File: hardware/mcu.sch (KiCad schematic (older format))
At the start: 29 parts, among them J1 Micro_SD_Card, J2 BOOT0, J3 Conn_01x04_Male, J5 Conn_01x03_Male, J6 display, SW1 SW_right, SW2 SW_right, SW3 SW_top, SW4 SW_middle, SW5 SW_bot, SW6 SW_Left, SW7 SW_middle2, U1 STM32F042C6Tx

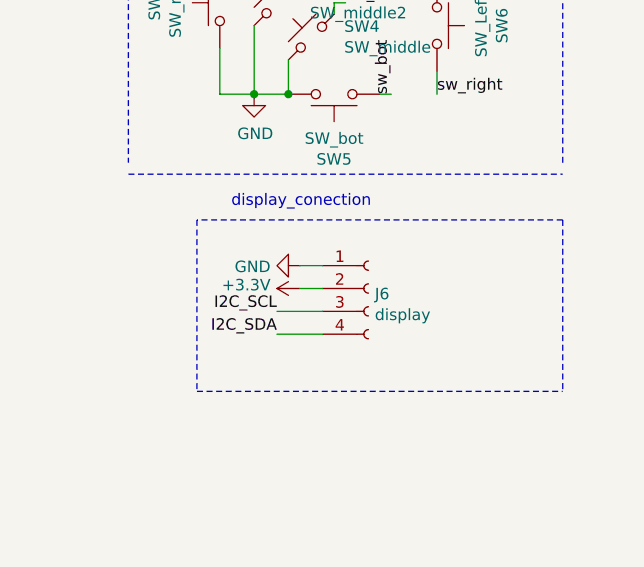
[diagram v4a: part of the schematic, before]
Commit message: Dodenie pullup do spi i i2c
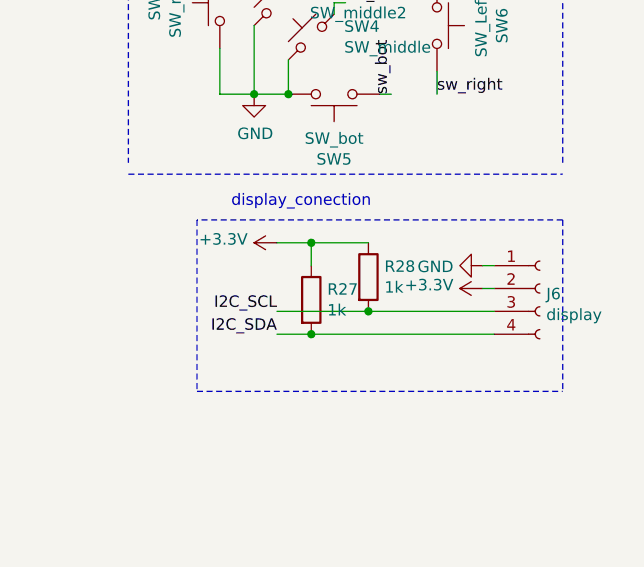
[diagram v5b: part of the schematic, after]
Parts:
- added R27, R28: 1k, Resistor_SMD:R_0603_1608Metric_Pad1.05x0.95mm_HandSolder, symbol Device:R
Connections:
- net +3V3: now also R27.1, R28.1
- net I2C_SCL: now also R28.2
- net I2C_SDA: now also R27.2
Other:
- moved on the sheet: J6
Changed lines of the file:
@@
 L power:GND #PWR?
 U 1 1 5D235C25
-P 8650 4700
+P 9450 4700
 AR Path="/5CDEAC68/5D235C25" Ref="#PWR?"  Part="1"
 AR Path="/5CDEAB6D/5D235C25" Ref="#PWR0139"  Part="1"
-F 0 "#PWR0139" H 8650 4450 50  0001 C CNN
-F 1 "GND" V 8655 4572 50  0000 R CNN
-F 2 "" H 8650 4700 50  0001 C CNN
-F 3 "" H 8650 4700 50  0001 C CNN
-	1    8650 4700
+F 0 "#PWR0139" H 9450 4450 50  0001 C CNN
+F 1 "GND" V 9455 4572 50  0000 R CNN
+F 2 "" H 9450 4700 50  0001 C CNN
+F 3 "" H 9450 4700 50  0001 C CNN
+	1    9450 4700
 	0    1    1    0
-$EndComp
-$Comp
-L power:+3.3V #PWR?
-U 1 1 5D235C2B
-P 8650 4800
-AR Path="/5CDEAC68/5D235C2B" Ref="#PWR?"  Part="1"
-AR Path="/5CDEAB6D/5D235C2B" Ref="#PWR0141"  Part="1"
-F 0 "#PWR0141" H 8650 4650 50  0001 C CNN
-F 1 "+3.3V" V 8665 4928 50  0000 L CNN
-F 2 "" H 8650 4800 50  0001 C CNN
-F 3 "" H 8650 4800 50  0001 C CNN
-	1    8650 4800
-	0    -1   -1   0
 $EndComp
 Text Label 8550 4900 2    50   ~ 0
@@
 L Connector:Conn_01x04_Female J6
 U 1 1 5D24C80E
-P 8950 4800
-F 0 "J6" H 8978 4776 50  0000 L CNN
-F 1 "display" H 8978 4685 50  0000 L CNN
-F 2 "Connector_PinSocket_2.54mm:PinSocket_1x04_P2.54mm_Vertical" H 8950 4800 50  0001 C CNN
-F 3 "~" H 8950 4800 50  0001 C CNN
-	1    8950 4800
+P 9700 4800
+F 0 "J6" H 9728 4776 50  0000 L CNN
+F 1 "display" H 9728 4685 50  0000 L CNN
+F 2 "Connector_PinSocket_2.54mm:PinSocket_1x04_P2.54mm_Vertical" H 9700 4800 50  0001 C CNN
+F 3 "~" H 9700 4800 50  0001 C CNN
+	1    9700 4800
 	1    0    0    -1
 $EndComp
 Wire Wire Line
-	8550 4900 8750 4900
+	9450 4700 9500 4700
 Wire Wire Line
-	8750 4800 8650 4800
-Wire Wire Line
-	8650 4700 8750 4700
-Wire Wire Line
-	8750 5000 8550 5000
+	9500 5000 8700 5000
 Text Notes 8350 4450 0    50   ~ 0
 display_conection
@@
 Text Notes 1500 3000 0    50   ~ 0
 programing connection\n
+Wire Wire Line
+	9500 4800 9450 4800
+$Comp
+L power:+3.3V #PWR?
+U 1 1 5D235C2B
+P 9450 4800
+AR Path="/5CDEAC68/5D235C2B" Ref="#PWR?"  Part="1"
+AR Path="/5CDEAB6D/5D235C2B" Ref="#PWR0141"  Part="1"
+F 0 "#PWR0141" H 9450 4650 50  0001 C CNN
+F 1 "+3.3V" V 9465 4928 50  0000 L CNN
+F 2 "" H 9450 4800 50  0001 C CNN
+F 3 "" H 9450 4800 50  0001 C CNN
+	1    9450 4800
+	0    -1   -1   0
+$EndComp
+$Comp
+L Device:R R27
+U 1 1 5D3198A1
+P 8700 4850
+F 0 "R27" H 8770 4896 50  0000 L CNN
+F 1 "1k" H 8770 4805 50  0000 L CNN
+F 2 "Resistor_SMD:R_0603_1608Metric_Pad1.05x0.95mm_HandSolder" V 8630 4850 50  0001 C CNN
+F 3 "~" H 8700 4850 50  0001 C CNN
+	1    8700 4850
+	1    0    0    -1
+$EndComp
+Connection ~ 8700 5000
+Wire Wire Line
+	8700 5000 8550 5000
+$Comp
+L Device:R R28
+U 1 1 5D319E5F
+P 8950 4750
+F 0 "R28" H 9020 4796 50  0000 L CNN
+F 1 "1k" H 9020 4705 50  0000 L CNN
+F 2 "Resistor_SMD:R_0603_1608Metric_Pad1.05x0.95mm_HandSolder" V 8880 4750 50  0001 C CNN
+F 3 "~" H 8950 4750 50  0001 C CNN
+	1    8950 4750
+	1    0    0    -1
+$EndComp
+$Comp
+L power:+3.3V #PWR?
+U 1 1 5D31ED2B
+P 8550 4600
+AR Path="/5CDEAC68/5D31ED2B" Ref="#PWR?"  Part="1"
+AR Path="/5CDEAB6D/5D31ED2B" Ref="#PWR0142"  Part="1"
+F 0 "#PWR0142" H 8550 4450 50  0001 C CNN
+F 1 "+3.3V" V 8565 4728 50  0000 L CNN
+F 2 "" H 8550 4600 50  0001 C CNN
+F 3 "" H 8550 4600 50  0001 C CNN
+	1    8550 4600
+	0    -1   -1   0
+$EndComp
+Wire Wire Line
+	8550 4600 8700 4600
+Wire Wire Line
+	8700 4700 8700 4600
+Connection ~ 8700 4600
+Connection ~ 8950 4900
+Wire Wire Line
+	8950 4900 9500 4900
+Wire Wire Line
+	8550 4900 8950 4900
+Wire Wire Line
+	8700 4600 8950 4600
 $EndSCHEMATC

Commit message: pierwszy układ PCB
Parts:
- added R32, R33: 47, Resistor_SMD:R_0603_1608Metric_Pad1.05x0.95mm_HandSolder, symbol Device:R
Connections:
- net POTMOSI: now also R33.2; no longer U1.41 (PB5)
- net POTSCK: now also R32.2; no longer U1.39 (PB3)
- new net: R32.1, U1.39 (PB3)
- new net: R33.1, U1.41 (PB5)
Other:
- moved on the sheet: R27, R28
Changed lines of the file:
@@
 Wire Wire Line
 	5250 5300 4900 5300
-Text HLabel 4800 4100 0    50   Output ~ 0
+Text HLabel 4400 4100 0    50   Output ~ 0
 POTSCK
-Text HLabel 4800 4300 0    50   Output ~ 0
-POTMOSI
-Wire Wire Line
-	4800 4100 5250 4100
-Wire Wire Line
-	5250 4300 4800 4300
-Text Label 4900 4100 0    50   ~ 0
-POTSCK
-Text Label 4900 4300 0    50   ~ 0
+Text HLabel 4400 4300 0    50   Output ~ 0
 POTMOSI
 Text Label 4950 4200 0    50   ~ 0
 POTSS
 Wire Wire Line
-	5250 4200 4800 4200
-Text HLabel 4800 4200 0    50   Output ~ 0
+	5250 4200 4400 4200
+Text HLabel 4400 4200 0    50   Output ~ 0
 POTCS
 Wire Wire Line
@@
 ADC6
 Wire Wire Line
-	5250 4400 4850 4400
-Wire Wire Line
-	5250 4500 4850 4500
-Text HLabel 4850 4400 0    50   Output ~ 0
+	5250 4400 4400 4400
+Wire Wire Line
+	5250 4500 4400 4500
+Text HLabel 4400 4400 0    50   Output ~ 0
 POTRST
 Text Label 4950 4400 0    50   ~ 0
@@
 	0    1    1    0
 $EndComp
-Text HLabel 4850 4500 0    50   Output ~ 0
+Text HLabel 4400 4500 0    50   Output ~ 0
 POTSHDN
 Wire Wire Line
@@
 	9450 4700 9500 4700
 Wire Wire Line
-	9500 5000 8700 5000
+	9500 5000 8650 5000
 Text Notes 8350 4450 0    50   ~ 0
 display_conection
@@
 	0    -1   -1   0
 $EndComp
-$Comp
-L Device:R R27
-U 1 1 5D3198A1
-P 8700 4850
-F 0 "R27" H 8770 4896 50  0000 L CNN
-F 1 "1k" H 8770 4805 50  0000 L CNN
-F 2 "Resistor_SMD:R_0603_1608Metric_Pad1.05x0.95mm_HandSolder" V 8630 4850 50  0001 C CNN
-F 3 "~" H 8700 4850 50  0001 C CNN
-	1    8700 4850
-	1    0    0    -1
-$EndComp
-Connection ~ 8700 5000
-Wire Wire Line
-	8700 5000 8550 5000
+Connection ~ 8650 5000
 $Comp
 L Device:R R28
 U 1 1 5D319E5F
-P 8950 4750
-F 0 "R28" H 9020 4796 50  0000 L CNN
-F 1 "1k" H 9020 4705 50  0000 L CNN
-F 2 "Resistor_SMD:R_0603_1608Metric_Pad1.05x0.95mm_HandSolder" V 8880 4750 50  0001 C CNN
-F 3 "~" H 8950 4750 50  0001 C CNN
-	1    8950 4750
+P 8900 4750
+F 0 "R28" H 8970 4796 50  0000 L CNN
+F 1 "1k" H 8970 4705 50  0000 L CNN
+F 2 "Resistor_SMD:R_0603_1608Metric_Pad1.05x0.95mm_HandSolder" V 8830 4750 50  0001 C CNN
+F 3 "~" H 8900 4750 50  0001 C CNN
+	1    8900 4750
 	1    0    0    -1
 $EndComp
@@
 $EndComp
 Wire Wire Line
-	8550 4600 8700 4600
-Wire Wire Line
-	8700 4700 8700 4600
-Connection ~ 8700 4600
-Connection ~ 8950 4900
-Wire Wire Line
-	8950 4900 9500 4900
-Wire Wire Line
-	8550 4900 8950 4900
-Wire Wire Line
-	8700 4600 8950 4600
+	8550 4600 8650 4600
+Wire Wire Line
+	8650 4700 8650 4600
+Connection ~ 8650 4600
+Connection ~ 8900 4900
+Wire Wire Line
+	8900 4900 9500 4900
+Wire Wire Line
+	8550 4900 8900 4900
+Wire Wire Line
+	8650 4600 8900 4600
+$Comp
+L Device:R R32
+U 1 1 5D460BB7
+P 4700 4100
+F 0 "R32" V 4493 4100 50  0000 C CNN
+F 1 "47" V 4584 4100 50  0000 C CNN
+F 2 "Resistor_SMD:R_0603_1608Metric_Pad1.05x0.95mm_HandSolder" V 4630 4100 50  0001 C CNN
+F 3 "~" H 4700 4100 50  0001 C CNN
+	1    4700 4100
+	0    1    1    0
+$EndComp
+$Comp
+L Device:R R33
+U 1 1 5D4611CB
+P 4700 4300
+F 0 "R33" V 4493 4300 50  0000 C CNN
+F 1 "47" V 4584 4300 50  0000 C CNN
+F 2 "Resistor_SMD:R_0603_1608Metric_Pad1.05x0.95mm_HandSolder" V 4630 4300 50  0001 C CNN
+F 3 "~" H 4700 4300 50  0001 C CNN
+	1    4700 4300
+	0    1    1    0
+$EndComp
+Wire Wire Line
+	4400 4300 4550 4300
+Wire Wire Line
+	4400 4100 4550 4100
+Wire Wire Line
+	4850 4100 5250 4100
+Wire Wire Line
+	5250 4300 4850 4300
+Wire Wire Line
+	8650 5000 8550 5000
+$Comp
+L Device:R R27
+U 1 1 5D3198A1
+P 8650 4850
+F 0 "R27" H 8720 4896 50  0000 L CNN
+F 1 "1k" H 8720 4805 50  0000 L CNN
+F 2 "Resistor_SMD:R_0603_1608Metric_Pad1.05x0.95mm_HandSolder" V 8580 4850 50  0001 C CNN
+F 3 "~" H 8650 4850 50  0001 C CNN
+	1    8650 4850
+	1    0    0    -1
+$EndComp
 $EndSCHEMATC

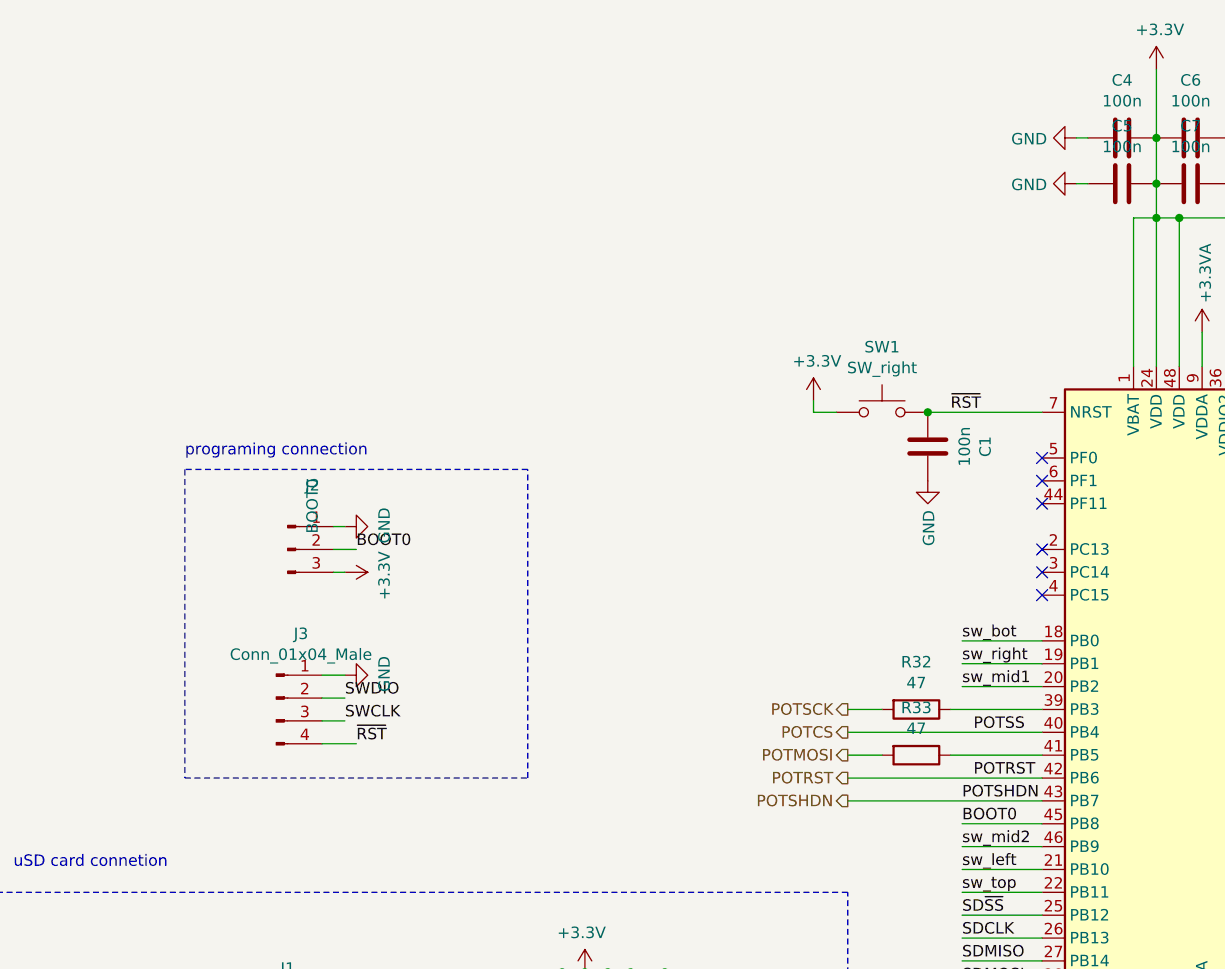
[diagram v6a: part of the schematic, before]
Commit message: update pinoutu, zmiany footprintów
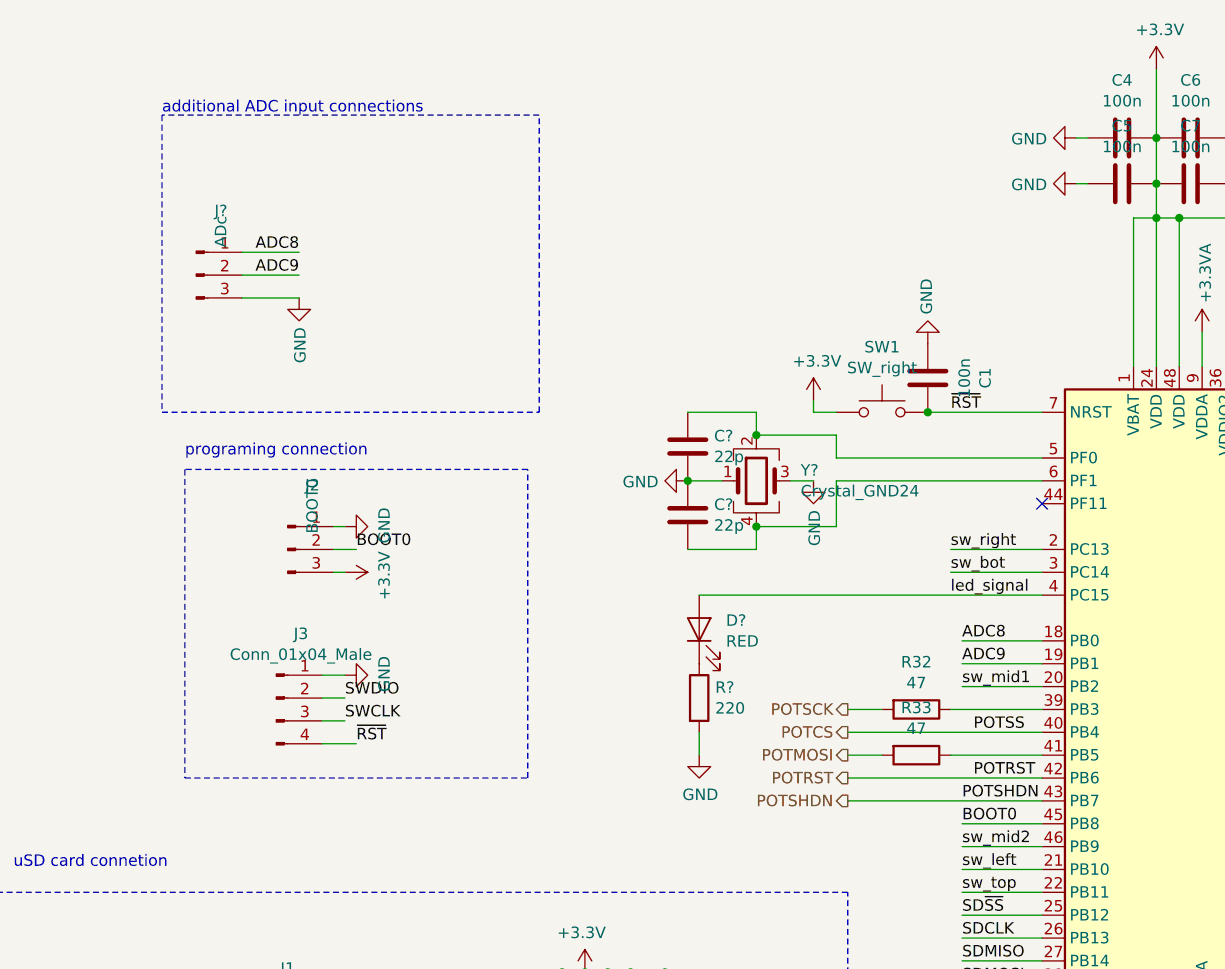
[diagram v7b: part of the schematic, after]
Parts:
- added C? (x2): 22p, symbol Device:C
- added D?: RED, LED_SMD:LED_0805_2012Metric, symbol Device:LED
- added J?: ADc, Connector_PinHeader_2.54mm:PinHeader_1x03_P2.54mm_Vertical, symbol Connector:Conn_01x03_Male
- added R?: 220, Resistor_SMD:R_0603_1608Metric_Pad1.05x0.95mm_HandSolder, symbol Device:R
- added Y?: Crystal_GND24, symbol Device:Crystal_GND24
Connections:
- net GND: now also C1.2, C?.1, C?.2, J?.3 (Pin_3), R?.2, Y?.1, Y?.3; no longer C1.1
- net sw_bot: now also U1.3 (PC14); no longer U1.18 (PB0)
- net sw_right: now also U1.2 (PC13); no longer U1.19 (PB1)
- net ~RST: now also C1.1; no longer C1.2
- net led_signal: now reaches U1.4 (PC15)
- net led_signal: now also D?.2 (A)
- net at U1.5 (PF0): now also C?.1, Y?.2
- net at U1.6 (PF1): now also C?.2, Y?.4
- new net: D?.1 (K), R?.1
- new net ADC8: J?.1 (Pin_1), U1.18 (PB0)
- new net ADC9: J?.2 (Pin_2), U1.19 (PB1)
- no-connect marks 7 -> 2
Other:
- note added: "additional ADC input connections\n"
- moved on the sheet: C1
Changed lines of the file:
@@
 	4100 6250 3600 6250
 Connection ~ 3600 6250
-$Comp
-L MCU_ST_STM32F0:STM32F042C6Tx U1
-U 1 1 5D61AD1D
-P 5850 4000
-F 0 "U1" H 5850 2411 50  0000 C CNN
-F 1 "STM32F042C6Tx" H 5850 2320 50  0000 C CNN
-F 2 "Package_QFP:LQFP-48_7x7mm_P0.5mm" H 5350 2600 50  0001 R CNN
-F 3 "http://www.st.com/st-web-ui/static/active/en/resource/technical/document/datasheet/DM00105814.pdf" H 5850 4000 50  0001 C CNN
-	1    5850 4000
-	1    0    0    -1
-$EndComp
 Wire Wire Line
 	5650 2600 5650 1950
@@
 Text Label 6500 4500 0    50   ~ 0
 ADC7
-Text HLabel 6700 3800 2    50   Output ~ 0
-ADC0
 Text HLabel 6700 3900 2    50   Output ~ 0
 ADC1
@@
 Text Label 4900 4000 0    50   ~ 0
 sw_mid1
-Text Label 4900 3900 0    50   ~ 0
+Text Label 4850 3400 0    50   ~ 0
 sw_right
-Text Label 4900 3800 0    50   ~ 0
+Text Label 4850 3500 0    50   ~ 0
 sw_bot
 $Comp
 L Device:C C1
 U 1 1 5CE5A2EA
-P 4750 2950
-F 0 "C1" V 4498 2950 50  0000 C CNN
-F 1 "100n" V 4589 2950 50  0000 C CNN
-F 2 "Capacitor_SMD:C_0603_1608Metric_Pad1.05x0.95mm_HandSolder" H 4788 2800 50  0001 C CNN
-F 3 "~" H 4750 2950 50  0001 C CNN
-	1    4750 2950
+P 4750 2650
+F 0 "C1" V 4498 2650 50  0000 C CNN
+F 1 "100n" V 4589 2650 50  0000 C CNN
+F 2 "Capacitor_SMD:C_0603_1608Metric_Pad1.05x0.95mm_HandSolder" H 4788 2500 50  0001 C CNN
+F 3 "~" H 4750 2650 50  0001 C CNN
+	1    4750 2650
 	-1   0    0    1
 $EndComp
@@
 L power:GND #PWR08
 U 1 1 5CE5FAB4
-P 4750 3100
-F 0 "#PWR08" H 4750 2850 50  0001 C CNN
-F 1 "GND" V 4755 2972 50  0000 R CNN
-F 2 "" H 4750 3100 50  0001 C CNN
-F 3 "" H 4750 3100 50  0001 C CNN
-	1    4750 3100
-	1    0    0    -1
+P 4750 2500
+F 0 "#PWR08" H 4750 2250 50  0001 C CNN
+F 1 "GND" V 4755 2372 50  0000 R CNN
+F 2 "" H 4750 2500 50  0001 C CNN
+F 3 "" H 4750 2500 50  0001 C CNN
+	1    4750 2500
+	-1   0    0    1
 $EndComp
 Text Label 4850 2800 0    50   ~ 0
@@
 	1    0    0    -1
 $EndComp
-Connection ~ 4750 2800
 $Comp
 L power:+3.3V #PWR07
@@
 Wire Wire Line
 	6450 4900 6850 4900
-NoConn ~ 5250 3000
-NoConn ~ 5250 3100
 NoConn ~ 5250 3200
-NoConn ~ 5250 3400
-NoConn ~ 5250 3500
-NoConn ~ 5250 3600
 $Comp
 L power:GNDA #PWR022
@@
 	1    0    0    -1
 $EndComp
+Text HLabel 6700 3800 2    50   Output ~ 0
+ADC0
+Text Label 4900 3800 0    50   ~ 0
+ADC8
+Text Label 4900 3900 0    50   ~ 0
+ADC9
+Wire Wire Line
+	5250 3400 4850 3400
+Wire Wire Line
+	4850 3500 5250 3500
+$Comp
+L Connector:Conn_01x03_Male J?
+U 1 1 5CE37969
+P 1550 2200
+F 0 "J?" H 1658 2481 50  0000 C CNN
+F 1 "ADc" V 1658 2390 50  0000 C CNN
+F 2 "Connector_PinHeader_2.54mm:PinHeader_1x03_P2.54mm_Vertical" H 1550 2200 50  0001 C CNN
+F 3 "~" H 1550 2200 50  0001 C CNN
+	1    1550 2200
+	1    0    0    -1
+$EndComp
+Wire Notes Line
+	1400 2800 3050 2800
+Wire Notes Line
+	3050 2800 3050 1500
+Wire Notes Line
+	3050 1500 1400 1500
+Wire Notes Line
+	1400 1500 1400 2800
+Text Notes 1400 1500 0    50   ~ 0
+additional ADC input connections\n
+$Comp
+L power:GND #PWR?
+U 1 1 5CE448F6
+P 2000 2300
+F 0 "#PWR?" H 2000 2050 50  0001 C CNN
+F 1 "GND" V 2005 2172 50  0000 R CNN
+F 2 "" H 2000 2300 50  0001 C CNN
+F 3 "" H 2000 2300 50  0001 C CNN
+	1    2000 2300
+	1    0    0    -1
+$EndComp
+Text Label 2000 2100 2    50   ~ 0
+ADC8
+Wire Wire Line
+	1750 2100 2000 2100
+Wire Wire Line
+	1750 2200 2000 2200
+Wire Wire Line
+	2000 2300 1750 2300
+Text Label 2000 2200 2    50   ~ 0
+ADC9
+$Comp
+L Device:Crystal_GND24 Y?
+U 1 1 5CE5951A
+P 4000 3100
+F 0 "Y?" H 4194 3146 50  0000 L CNN
+F 1 "Crystal_GND24" H 4194 3055 50  0000 L CNN
+F 2 "" H 4000 3100 50  0001 C CNN
+F 3 "https://www.tme.eu/pl/details/abm8-16.000mhz-b2/rezonatory-kwarcowe-smd/abracon/abm8-16-000mhz-b2-t/" H 4000 3100 50  0001 C CNN
+	1    4000 3100
+	1    0    0    -1
+$EndComp
+$Comp
+L MCU_ST_STM32F0:STM32F042C6Tx U1
+U 1 1 5D61AD1D
+P 5850 4000
+F 0 "U1" H 5850 2411 50  0000 C CNN
+F 1 "STM32F042C6Tx" H 5850 2320 50  0000 C CNN
+F 2 "Package_QFP:LQFP-48_7x7mm_P0.5mm" H 5350 2600 50  0001 R CNN
+F 3 "http://www.st.com/st-web-ui/static/active/en/resource/technical/document/datasheet/DM00105814.pdf" H 5850 4000 50  0001 C CNN
+	1    5850 4000
+	1    0    0    -1
+$EndComp
+Connection ~ 4750 2800
+Wire Wire Line
+	5250 3000 4350 3000
+Wire Wire Line
+	4350 3000 4350 2900
+Wire Wire Line
+	4350 2900 4000 2900
+Wire Wire Line
+	4000 3300 4350 3300
+Wire Wire Line
+	4350 3300 4350 3100
+Wire Wire Line
+	4350 3100 5250 3100
+$Comp
+L Device:C C?
+U 1 1 5CE8BF2D
+P 3700 2950
+F 0 "C?" H 3815 2996 50  0000 L CNN
+F 1 "22p" H 3815 2905 50  0000 L CNN
+F 2 "" H 3738 2800 50  0001 C CNN
+F 3 "~" H 3700 2950 50  0001 C CNN
+	1    3700 2950
+	1    0    0    -1
+$EndComp
+$Comp
+L Device:C C?
+U 1 1 5CE8C2A0
+P 3700 3250
+F 0 "C?" H 3815 3296 50  0000 L CNN
+F 1 "22p" H 3815 3205 50  0000 L CNN
+F 2 "" H 3738 3100 50  0001 C CNN
+F 3 "~" H 3700 3250 50  0001 C CNN
+	1    3700 3250
+	1    0    0    -1
+$EndComp
+$Comp
+L power:GND #PWR?
+U 1 1 5CE8CAB4
+P 4250 3100
+F 0 "#PWR?" H 4250 2850 50  0001 C CNN
+F 1 "GND" V 4255 2972 50  0000 R CNN
+F 2 "" H 4250 3100 50  0001 C CNN
+F 3 "" H 4250 3100 50  0001 C CNN
+	1    4250 3100
+	1    0    0    -1
+$EndComp
+Wire Wire Line
+	4250 3100 4150 3100
+$Comp
+L power:GND #PWR?
+U 1 1 5CE9AAA5
+P 3700 3100
+F 0 "#PWR?" H 3700 2850 50  0001 C CNN
+F 1 "GND" V 3705 2972 50  0000 R CNN
+F 2 "" H 3700 3100 50  0001 C CNN
+F 3 "" H 3700 3100 50  0001 C CNN
+	1    3700 3100
+	0    1    1    0
+$EndComp
+Connection ~ 3700 3100
+Wire Wire Line
+	3700 3400 4000 3400
+Wire Wire Line
+	4000 3400 4000 3300
+Wire Wire Line
+	3700 3100 3850 3100
+Connection ~ 4000 3300
+Wire Wire Line
+	3700 2800 4000 2800
+Wire Wire Line
+	4000 2800 4000 2900
+Connection ~ 4000 2900
+$Comp
+L Device:LED D?
+U 1 1 5CEC06DD
+P 3750 3750
+F 0 "D?" V 3789 3633 50  0000 R CNN
+F 1 "RED" V 3698 3633 50  0000 R CNN
+F 2 "LED_SMD:LED_0805_2012Metric" H 3750 3750 50  0001 C CNN
+F 3 "~" H 3750 3750 50  0001 C CNN
+	1    3750 3750
+	0    -1   -1   0
+$EndComp
+$Comp
+L Device:R R?
+U 1 1 5CEC06E3
+P 3750 4050
+F 0 "R?" H 3820 4096 50  0000 L CNN
+F 1 "220" H 3820 4005 50  0000 L CNN
+F 2 "Resistor_SMD:R_0603_1608Metric_Pad1.05x0.95mm_HandSolder" V 3680 4050 50  0001 C CNN
+F 3 "~" H 3750 4050 50  0001 C CNN
+	1    3750 4050
+	1    0    0    -1
+$EndComp
+$Comp
+L power:GND #PWR?
+U 1 1 5CEC06E9
+P 3750 4300
+F 0 "#PWR?" H 3750 4050 50  0001 C CNN
+F 1 "GND" H 3755 4127 50  0000 C CNN
+F 2 "" H 3750 4300 50  0001 C CNN
+F 3 "" H 3750 4300 50  0001 C CNN
+	1    3750 4300
+	1    0    0    -1
+$EndComp
+Wire Wire Line
+	3750 4300 3750 4200
+Wire Wire Line
+	5250 3600 3750 3600
+Text Label 4850 3600 0    50   ~ 0
+led_signal
 $EndSCHEMATC
